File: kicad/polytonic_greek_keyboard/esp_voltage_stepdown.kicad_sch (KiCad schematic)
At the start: 5 parts, among them U3 TPS62162DSG

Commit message: [UPDATE] the board desing, [FIX] connection issues
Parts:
- C6: footprint Capacitor_SMD:C_0805_2012Metric -> Capacitor_SMD:C_0805_2012Metric_Pad1.18x1.45mm_HandSolder
- C7: footprint Capacitor_SMD:C_1206_3216Metric -> Capacitor_SMD:C_1206_3216Metric_Pad1.33x1.80mm_HandSolder
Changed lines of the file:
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@@
 			)
 		)
-		(property "Footprint" "Capacitor_SMD:C_0805_2012Metric"
+		(property "Footprint" "Capacitor_SMD:C_0805_2012Metric_Pad1.18x1.45mm_HandSolder"
 			(at 41.91 25.4 0)
 			(effects
@@
 			)
 		)
-		(property "Footprint" "Capacitor_SMD:C_1206_3216Metric"
+		(property "Footprint" "Capacitor_SMD:C_1206_3216Metric_Pad1.33x1.80mm_HandSolder"
 			(at 97.79 29.845 0)
 			(effects

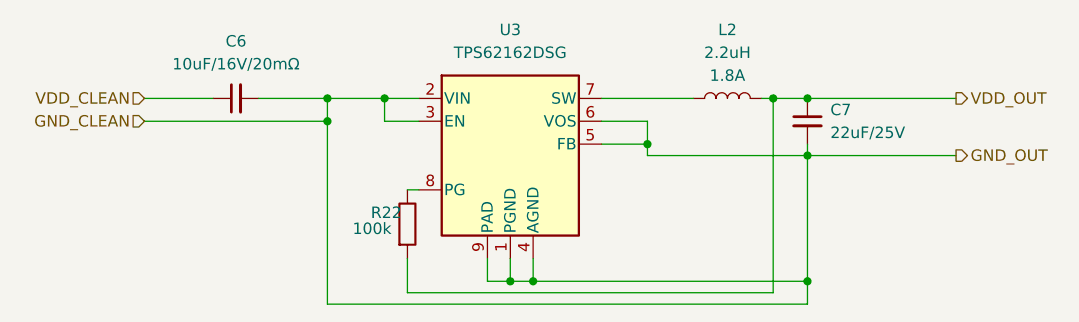
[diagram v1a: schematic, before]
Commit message: [UPDATE] the desing to fit on two separate pcbs
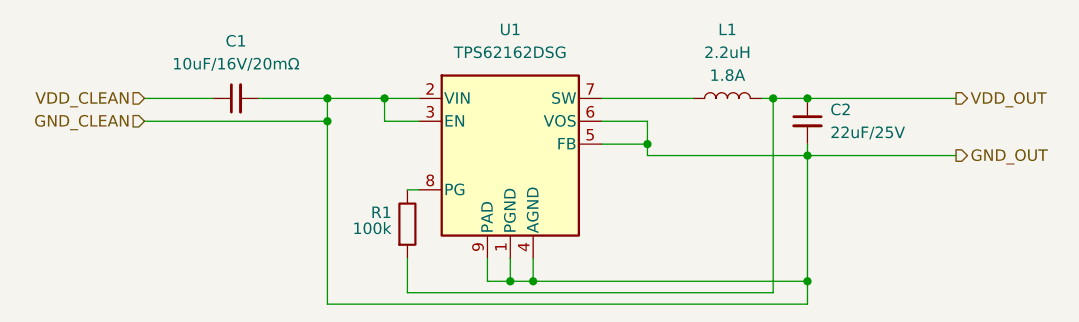
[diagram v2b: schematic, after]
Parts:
- renumbered C6 to C1, C7 to C2, L2 to L1, R22 to R1, U3 to U1
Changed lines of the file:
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@@
 		(dnp no)
 		(fields_autoplaced yes)
-		(property "Reference" "C6"
+		(property "Reference" "C1"
 			(at 36.8363 16.51 90)
 			(effects
@@
 		)
 		(instances
-			(project ""
-				(path "/cbe25a1b-6c02-43c2-9ff9-ba274c7cf6a2/7d9047f3-7c3b-4bc8-9296-0f56f4397655"
-					(reference "C6")
+			(project "polytonic_greek_keyboard"
+				(path "/cbe25a1b-6c02-43c2-9ff9-ba274c7cf6a2/8498b325-11fd-4b20-a704-75ec3d8987ef/3e13680f-afbf-4059-ae13-3c3d5e01d0cf"
+					(reference "C1")
 					(unit 1)
 				)
@@
 		(dnp no)
 		(fields_autoplaced yes)
-		(property "Reference" "L2"
+		(property "Reference" "L1"
 			(at 91.44 15.24 90)
 			(effects
@@
 		)
 		(instances
-			(project ""
-				(path "/cbe25a1b-6c02-43c2-9ff9-ba274c7cf6a2/7d9047f3-7c3b-4bc8-9296-0f56f4397655"
-					(reference "L2")
+			(project "polytonic_greek_keyboard"
+				(path "/cbe25a1b-6c02-43c2-9ff9-ba274c7cf6a2/8498b325-11fd-4b20-a704-75ec3d8987ef/3e13680f-afbf-4059-ae13-3c3d5e01d0cf"
+					(reference "L1")
 					(unit 1)
 				)
@@
 		(dnp no)
 		(fields_autoplaced yes)
-		(property "Reference" "C7"
+		(property "Reference" "C2"
 			(at 102.87 24.1362 0)
 			(effects
@@
 		)
 		(instances
-			(project ""
-				(path "/cbe25a1b-6c02-43c2-9ff9-ba274c7cf6a2/7d9047f3-7c3b-4bc8-9296-0f56f4397655"
-					(reference "C7")
+			(project "polytonic_greek_keyboard"
+				(path "/cbe25a1b-6c02-43c2-9ff9-ba274c7cf6a2/8498b325-11fd-4b20-a704-75ec3d8987ef/3e13680f-afbf-4059-ae13-3c3d5e01d0cf"
+					(reference "C2")
 					(unit 1)
 				)
@@
 		(on_board yes)
 		(dnp no)
-		(property "Reference" "R22"
+		(property "Reference" "R1"
 			(at 51.816 35.56 90)
 			(effects
@@
 		)
 		(instances
-			(project ""
-				(path "/cbe25a1b-6c02-43c2-9ff9-ba274c7cf6a2/7d9047f3-7c3b-4bc8-9296-0f56f4397655"
-					(reference "R22")
+			(project "polytonic_greek_keyboard"
+				(path "/cbe25a1b-6c02-43c2-9ff9-ba274c7cf6a2/8498b325-11fd-4b20-a704-75ec3d8987ef/3e13680f-afbf-4059-ae13-3c3d5e01d0cf"
+					(reference "R1")
 					(unit 1)
 				)
@@
 		(dnp no)
 		(fields_autoplaced yes)
-		(property "Reference" "U3"
+		(property "Reference" "U1"
 			(at 67.31 15.24 0)
 			(effects
@@
 		(instances
 			(project "polytonic_greek_keyboard"
-				(path "/cbe25a1b-6c02-43c2-9ff9-ba274c7cf6a2/7d9047f3-7c3b-4bc8-9296-0f56f4397655"
-					(reference "U3")
+				(path "/cbe25a1b-6c02-43c2-9ff9-ba274c7cf6a2/8498b325-11fd-4b20-a704-75ec3d8987ef/3e13680f-afbf-4059-ae13-3c3d5e01d0cf"
+					(reference "U1")
 					(unit 1)
 				)

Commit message: [UPDATE] anotation issues
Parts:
- renumbered C1 to C2, C2 to C3, R1 to R8, U1 to U2
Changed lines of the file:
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@@
 		(dnp no)
 		(fields_autoplaced yes)
-		(property "Reference" "C1"
+		(property "Reference" "C2"
 			(at 36.8363 16.51 90)
 			(effects
@@
 			(project "polytonic_greek_keyboard"
 				(path "/cbe25a1b-6c02-43c2-9ff9-ba274c7cf6a2/8498b325-11fd-4b20-a704-75ec3d8987ef/3e13680f-afbf-4059-ae13-3c3d5e01d0cf"
-					(reference "C1")
+					(reference "C2")
 					(unit 1)
 				)
@@
 		(dnp no)
 		(fields_autoplaced yes)
-		(property "Reference" "C2"
+		(property "Reference" "C3"
 			(at 102.87 24.1362 0)
 			(effects
@@
 			(project "polytonic_greek_keyboard"
 				(path "/cbe25a1b-6c02-43c2-9ff9-ba274c7cf6a2/8498b325-11fd-4b20-a704-75ec3d8987ef/3e13680f-afbf-4059-ae13-3c3d5e01d0cf"
-					(reference "C2")
+					(reference "C3")
 					(unit 1)
 				)
@@
 		(on_board yes)
 		(dnp no)
-		(property "Reference" "R1"
+		(property "Reference" "R8"
 			(at 51.816 35.56 90)
 			(effects
@@
 			(project "polytonic_greek_keyboard"
 				(path "/cbe25a1b-6c02-43c2-9ff9-ba274c7cf6a2/8498b325-11fd-4b20-a704-75ec3d8987ef/3e13680f-afbf-4059-ae13-3c3d5e01d0cf"
-					(reference "R1")
+					(reference "R8")
 					(unit 1)
 				)
@@
 		(dnp no)
 		(fields_autoplaced yes)
-		(property "Reference" "U1"
+		(property "Reference" "U2"
 			(at 67.31 15.24 0)
 			(effects
@@
 			(project "polytonic_greek_keyboard"
 				(path "/cbe25a1b-6c02-43c2-9ff9-ba274c7cf6a2/8498b325-11fd-4b20-a704-75ec3d8987ef/3e13680f-afbf-4059-ae13-3c3d5e01d0cf"
-					(reference "U1")
+					(reference "U2")
 					(unit 1)
 				)

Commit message: [UPDATE] the final merged version of the schematic before splitting into two separate kicad projects
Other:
- company: (none) -> Henry's Software House
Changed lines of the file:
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@@
 	(generator_version "9.0")
 	(paper "A4")
+	(title_block
+		(rev "1 - do not edit connector pin layout.")
+		(company "Henry's Software House")
+	)
 	(junction
 		(at 46.99 22.86)
